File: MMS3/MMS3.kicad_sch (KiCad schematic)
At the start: 3 parts

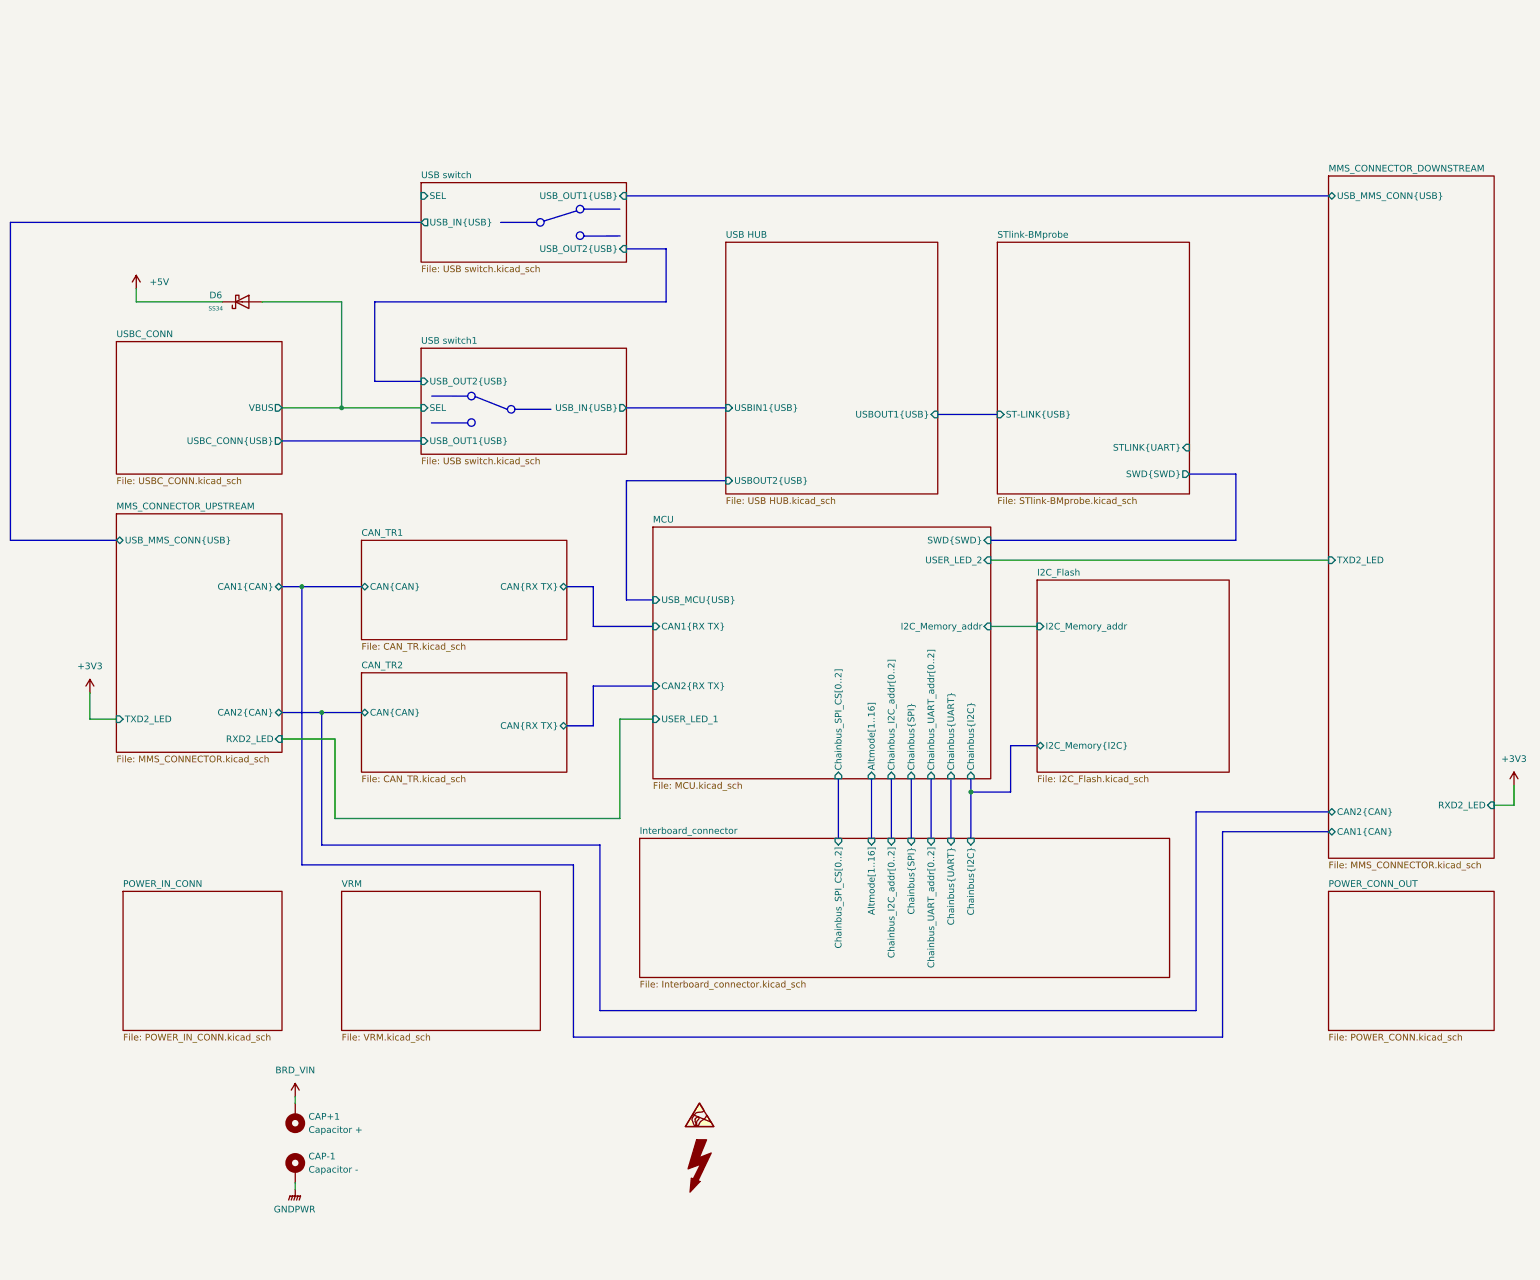
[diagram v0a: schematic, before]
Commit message: schematic + partly layout
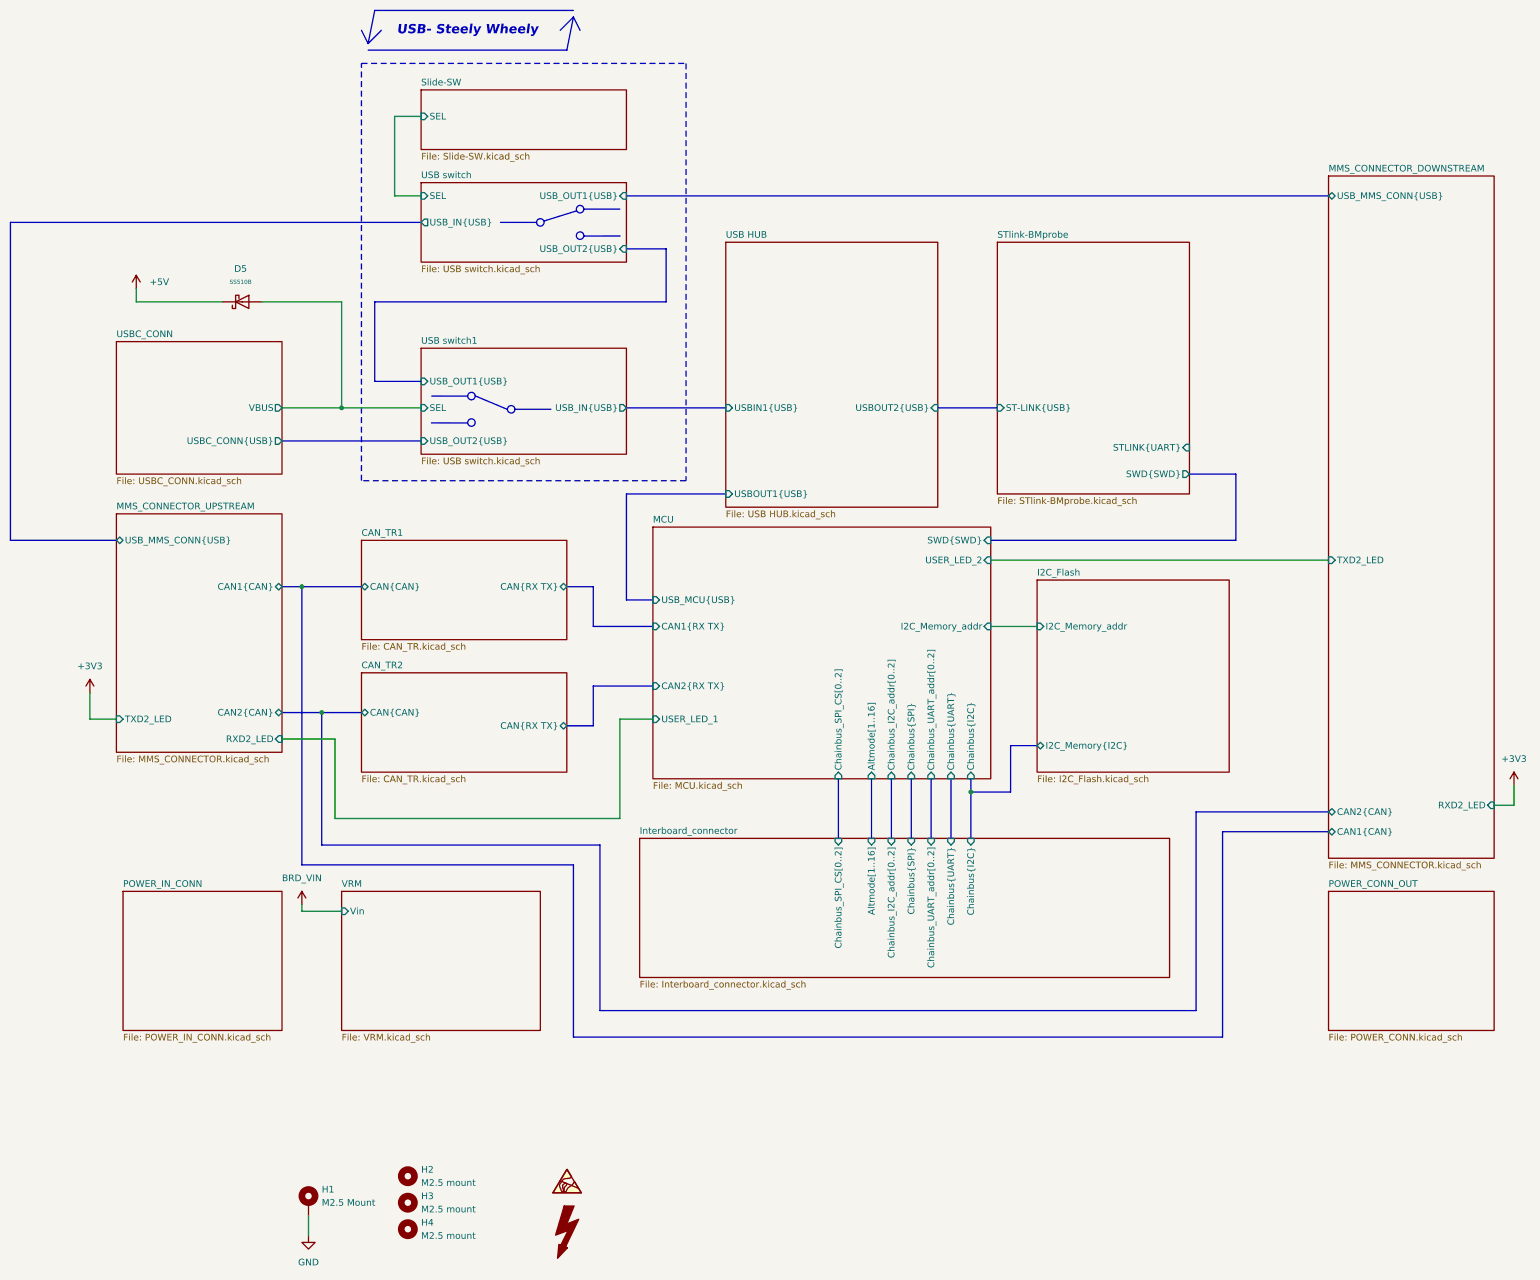
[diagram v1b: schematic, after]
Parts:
- removed CAP+1: Capacitor +, TestPoint:TestPoint_THTPad_1.5x1.5mm_Drill0.7mm, symbol Mechanical:MountingHole_Pad
- removed CAP-1: Capacitor -, TestPoint:TestPoint_THTPad_1.5x1.5mm_Drill0.7mm, symbol Mechanical:MountingHole_Pad
- removed D6: SS34, PCM_JLCPCB:D_SMA, symbol PCM_JLCPCB-Diodes:Schottky,SS34
- added D5: SS510B, PCM_JLCPCB:D_SMB, symbol PCM_JLCPCB-Diodes:Schottky,SS510B
- added H1: M2.5 Mount, MountingHole:MountingHole_2.7mm_M2.5_DIN965_Pad_TopOnly, symbol Mechanical:MountingHole_Pad
- added H2, H3, H4: M2.5 mount, MountingHole:MountingHole_2.7mm_M2.5, symbol Mechanical:MountingHole
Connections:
- net +5V: now also D5.1
- net USB switch1/SEL: now also D5.2
- new net GND: H1.1
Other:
- added sheet Slide-SW (Slide-SW.kicad_sch)
- sheet VRM ports: added Vin; removed none
- note added: "USB- Steely Wheely"

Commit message: almost done
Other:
- sheet Interboard_connector ports: added Chainbus_addr[0..7]; removed Chainbus_I2C_addr[0..2], Chainbus_SPI_CS[0..2], Chainbus_UART_addr[0..2]
- sheet MCU ports: added Chainbus_addr[0..7]; removed Chainbus_I2C_addr[0..2], Chainbus_SPI_CS[0..2], Chainbus_UART_addr[0..2]
- note added: "USB- Stealy Wheely"
- note removed: "USB- Steely Wheely"
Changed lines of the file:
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@@
 		)
 	)
-	(text "USB- Steely Wheely"
+	(text "USB- Stealy Wheely"
 		(exclude_from_sim no)
 		(at 132.08 25.4 0)
@@
 	(bus
 		(pts
-			(xy 217.17 168.91) (xy 217.17 180.34)
-		)
-		(stroke
-			(width 0)
-			(type default)
-		)
-	)
-	(bus
-		(pts
 			(xy 156.21 158.75) (xy 156.21 151.13)
 		)
@@
 	(bus
 		(pts
-			(xy 213.36 168.91) (xy 213.36 180.34)
+			(xy 104.14 156.21) (xy 111.76 156.21)
 		)
 		(stroke
@@
 	(bus
 		(pts
-			(xy 104.14 156.21) (xy 111.76 156.21)
+			(xy 220.98 168.91) (xy 220.98 180.34)
 		)
 		(stroke
@@
 	(bus
 		(pts
-			(xy 209.55 168.91) (xy 209.55 180.34)
-		)
-		(stroke
-			(width 0)
-			(type default)
-		)
-	)
-	(wire
-		(pts
-			(xy 68.58 77.47) (xy 85.09 77.47)
+			(xy 213.36 168.91) (xy 213.36 180.34)
 		)
 		(stroke
@@
 	(bus
 		(pts
-			(xy 236.22 162.56) (xy 236.22 171.45)
+			(xy 217.17 168.91) (xy 217.17 180.34)
 		)
 		(stroke
@@
 	(wire
 		(pts
-			(xy 59.69 157.48) (xy 64.77 157.48)
+			(xy 68.58 77.47) (xy 85.09 77.47)
 		)
 		(stroke
@@
 	(bus
 		(pts
-			(xy 203.2 168.91) (xy 203.2 180.34)
+			(xy 236.22 162.56) (xy 236.22 171.45)
 		)
 		(stroke
@@
 		)
 	)
-	(bus
+	(wire
 		(pts
-			(xy 220.98 168.91) (xy 220.98 180.34)
+			(xy 59.69 157.48) (xy 64.77 157.48)
 		)
 		(stroke
@@
 			)
 		)
-		(pin "Chainbus_UART_addr[0..2]" input
-			(at 220.98 180.34 90)
-			(effects
-				(font
-					(size 1.27 1.27)
-				)
-				(justify right)
-			)
-		)
 		(pin "Chainbus{SPI}" input
-			(at 217.17 180.34 90)
-			(effects
-				(font
-					(size 1.27 1.27)
-				)
-				(justify right)
-			)
-		)
-		(pin "Chainbus_I2C_addr[0..2]" input
-			(at 213.36 180.34 90)
+			(at 220.98 180.34 90)
 			(effects
 				(font
@@
 		)
 		(pin "Altmode[1..16]" input
-			(at 209.55 180.34 90)
+			(at 213.36 180.34 90)
 			(effects
 				(font
@@
 			)
 		)
-		(pin "Chainbus_SPI_CS[0..2]" input
-			(at 203.2 180.34 90)
+		(pin "Chainbus_addr[0..7]" input
+			(at 217.17 180.34 90)
 			(effects
 				(font
@@
 		)
 		(pin "Altmode[1..16]" input
-			(at 209.55 168.91 270)
+			(at 213.36 168.91 270)
 			(effects
 				(font
@@
 			)
 		)
-		(pin "Chainbus_SPI_CS[0..2]" input
-			(at 203.2 168.91 270)
-			(effects
-				(font
-					(size 1.27 1.27)
-				)
-				(justify left)
-			)
-		)
-		(pin "Chainbus_UART_addr[0..2]" input
-			(at 220.98 168.91 270)
-			(effects
-				(font
-					(size 1.27 1.27)
-				)
-				(justify left)
-			)
-		)
 		(pin "Chainbus{SPI}" input
-			(at 217.17 168.91 270)
-			(effects
-				(font
-					(size 1.27 1.27)
-				)
-				(justify left)
-			)
-		)
-		(pin "Chainbus_I2C_addr[0..2]" input
-			(at 213.36 168.91 270)
+			(at 220.98 168.91 270)
 			(effects
 				(font
@@
 			)
 		)
+		(pin "Chainbus_addr[0..7]" input
+			(at 217.17 168.91 270)
+			(effects
+				(font
+					(size 1.27 1.27)
+				)
+				(justify left)
+			)
+		)

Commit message: prod ready
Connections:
- no-connect marks 0 -> 2
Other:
- sheet MCU ports: added none; removed I2C_Memory_addr
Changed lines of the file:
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@@
 	)
 	(junction
+		(at 101.6 254)
+		(diameter 0)
+		(color 0 0 0 0)
+	)
+	(junction
 		(at 228.6 171.45)
 		(diameter 0)
@@
 		(color 0 0 0 0)
 	)
+	(no_connect
+		(at 237.49 139.7)
+	)
+	(no_connect
+		(at 275.59 105.41)
+	)
 	(wire
 		(pts
@@
 		)
 	)
+	(wire
+		(pts
+			(xy 92.71 252.73) (xy 92.71 254)
+		)
+		(stroke
+			(width 0)
+			(type default)
+		)
+	)
 	(polyline
 		(pts
@@
 		)
 	)
+	(wire
+		(pts
+			(xy 101.6 254) (xy 101.6 256.54)
+		)
+		(stroke
+			(width 0)
+			(type default)
+		)
+	)
 	(bus
 		(pts
@@
 	(bus
 		(pts
+			(xy 270.51 105.41) (xy 275.59 105.41)
+		)
+		(stroke
+			(width 0)
+			(type default)
+		)
+	)
+	(bus
+		(pts
 			(xy 156.21 151.13) (xy 167.64 151.13)
 		)
@@
 		)
 	)
-	(bus
+	(wire
 		(pts
-			(xy 156.21 132.08) (xy 156.21 139.7)
+			(xy 237.49 139.7) (xy 241.3 139.7)
 		)
 		(stroke
@@
 		)
 	)
-	(wire
+	(bus
 		(pts
-			(xy 107.95 194.31) (xy 100.33 194.31)
+			(xy 156.21 132.08) (xy 156.21 139.7)
 		)
 		(stroke
@@
 	(wire
 		(pts
-			(xy 232.41 139.7) (xy 241.3 139.7)
+			(xy 107.95 194.31) (xy 100.33 194.31)
 		)
 		(stroke
@@
 		)
 	)
+	(wire
+		(pts
+			(xy 101.6 254) (xy 92.71 254)
+		)
+		(stroke
+			(width 0)
+			(type default)
+		)
+	)
 	(polyline
 		(pts
@@
 	(wire
 		(pts
-			(xy 101.6 252.73) (xy 101.6 256.54)
+			(xy 101.6 252.73) (xy 101.6 254)
 		)
 		(stroke
@@
 	)
 	(symbol
+		(lib_id "power:PWR_FLAG")
+		(at 92.71 252.73 0)
+		(unit 1)
+		(body_style 1)
+		(exclude_from_sim no)
+		(in_bom yes)
+		(on_board yes)
+		(in_pos_files yes)
+		(dnp no)
+		(fields_autoplaced yes)
+		(property "Reference" "#FLG01"
+			(at 92.71 250.825 0)
+			(hide yes)
+			(show_name no)
+			(do_not_autoplace no)
+			(effects
+				(font
+					(size 1.27 1.27)
+				)
+			)
+		)
+		(property "Value" "PWR_FLAG"
+			(at 92.71 247.65 0)
+			(show_name no)
+			(do_not_autoplace no)
+			(effects
+				(font
+					(size 1.27 1.27)
+				)
+			)
+		)
+		(property "Footprint" ""
+			(at 92.71 252.73 0)
+			(hide yes)
+			(show_name no)
+			(do_not_autoplace no)
+			(effects
+				(font
+					(size 1.27 1.27)
+				)
+			)
+		)
+		(property "Datasheet" ""
+			(at 92.71 252.73 0)
+			(hide yes)
+			(show_name no)
+			(do_not_autoplace no)
+			(effects
+				(font
+					(size 1.27 1.27)
+				)
+			)
+		)
+		(property "Description" "Special symbol for telling ERC where power comes from"
+			(at 92.71 252.73 0)
+			(hide yes)
+			(show_name no)
+			(do_not_autoplace no)
+			(effects
+				(font
+					(size 1.27 1.27)
+				)
+			)
+		)
+		(pin "1"
+		)
+		(instances
+			(project "MMS3"
+				(path "/712cea22-140d-4c92-923f-f4998caf3ecd"
+					(reference "#FLG01")
+					(unit 1)
+				)
+			)
+		)
+	)
+	(symbol
 		(lib_id "Graphic:SYM_ESD_Small")
 		(at 151.13 246.38 0)
@@
 			)
 		)
-		(pin "I2C_Memory_addr" input
-			(at 232.41 139.7 0)
-			(effects
-				(font
-					(size 1.27 1.27)
-				)
-				(justify right)
-			)
-		)
